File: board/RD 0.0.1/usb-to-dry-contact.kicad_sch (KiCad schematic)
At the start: 11 parts, among them J1 480-37-1000, U1 CP2102N-Axx-xQFN28

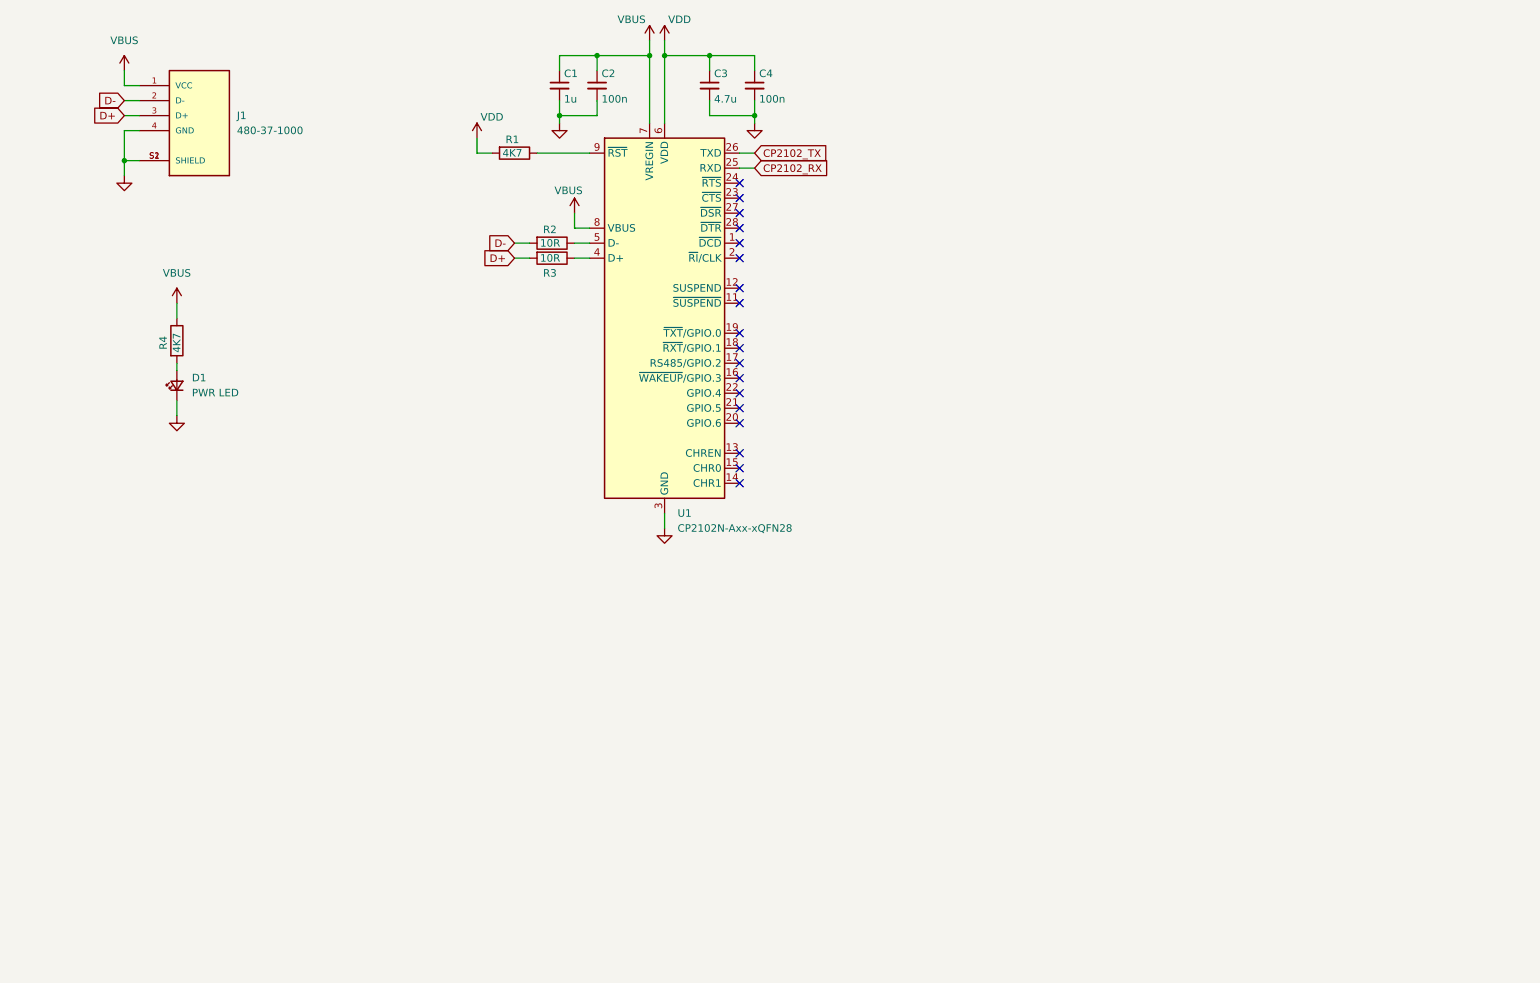
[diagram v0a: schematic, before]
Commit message: add relay, output conn, isp conn, avalanche diode
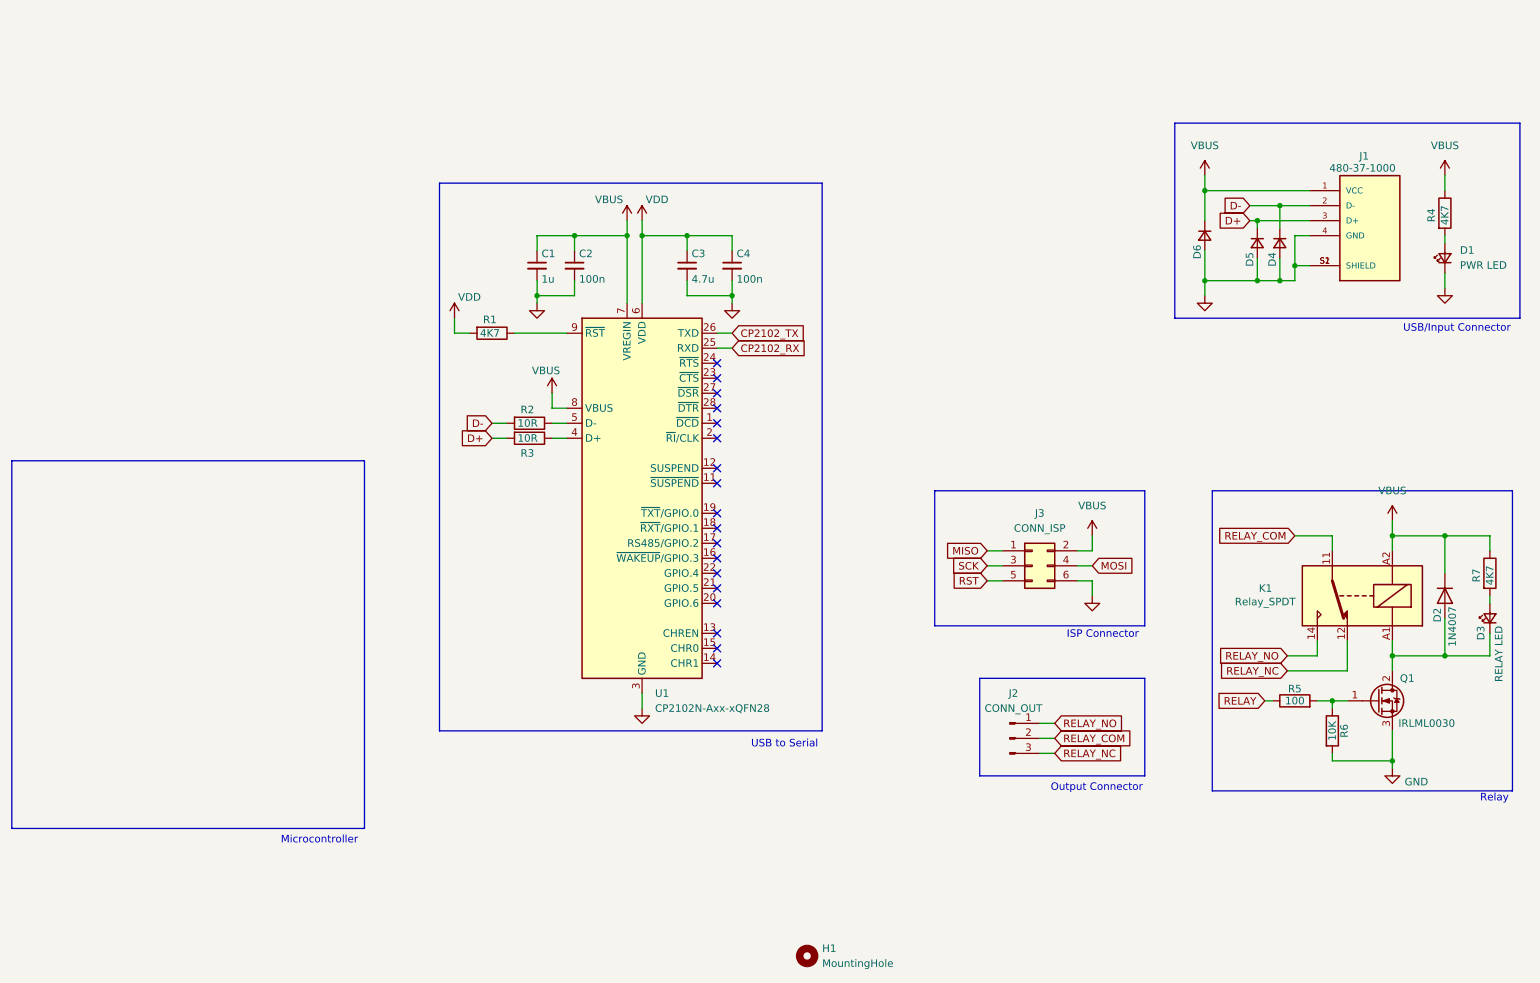
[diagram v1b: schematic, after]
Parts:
- added D2: 1N4007, Diode_SMD:D_SOD-123F, symbol Device:D
- added D3: RELAY LED, symbol Device:LED_Small
- added D4, D5, D6: D_Small, symbol Device:D_Small
- added H1: MountingHole, symbol Mechanical:MountingHole
- added J2: CONN_OUT, symbol Connector:Conn_01x03_Pin
- added J3: CONN_ISP, symbol Connector_Generic:Conn_02x03_Odd_Even
- added K1: Relay_SPDT, symbol Relay:Relay_SPDT
- added Q1: IRLML0030, Package_TO_SOT_SMD:SOT-23, symbol Transistor_FET:IRF540N
- added R5: 100, Resistor_SMD:R_0603_1608Metric_Pad0.98x0.95mm_HandSolder, symbol Device:R
- added R6: 10K, Resistor_SMD:R_0603_1608Metric_Pad0.98x0.95mm_HandSolder, symbol Device:R
- added R7: 4K7, symbol Device:R
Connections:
- net D+: now also D5.1 (K)
- net D-: now also D4.1 (K)
- net GND: now also D4.2 (A), D5.2 (A), D6.2 (A), J3.6 (Pin_6), Q1.3 (S), R6.2
- net VBUS: now also D2.1 (K), D6.1 (K), J3.2 (Pin_2), K1.A2, R7.1
- new net: Q1.1 (G), R5.2, R6.1
- new net: D2.2 (A), D3.1 (K), K1.A1, Q1.2 (D)
- new net: D3.2 (A), R7.2
- new net MISO: J3.1 (Pin_1)
- new net MOSI: J3.4 (Pin_4)
- new net RELAY: R5.1
- new net RELAY_COM: J2.2 (Pin_2), K1.11
- new net RELAY_NC: J2.3 (Pin_3), K1.12
- new net RELAY_NO: J2.1 (Pin_1), K1.14
- new net RST: J3.5 (Pin_5)
- new net SCK: J3.3 (Pin_3)
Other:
- note added: "ISP Connector"
- note added: "Microcontroller"
- note added: "Output Connector"
- note added: "Relay"
- note added: "USB to Serial"
- note added: "USB/Input Connector"
- moved on the sheet: C1, C2, C3, C4, D1, J1, R1, R2, R3, R4, U1

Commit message: add STM8 to sch, change the ISP to SWIM connector, place components to board
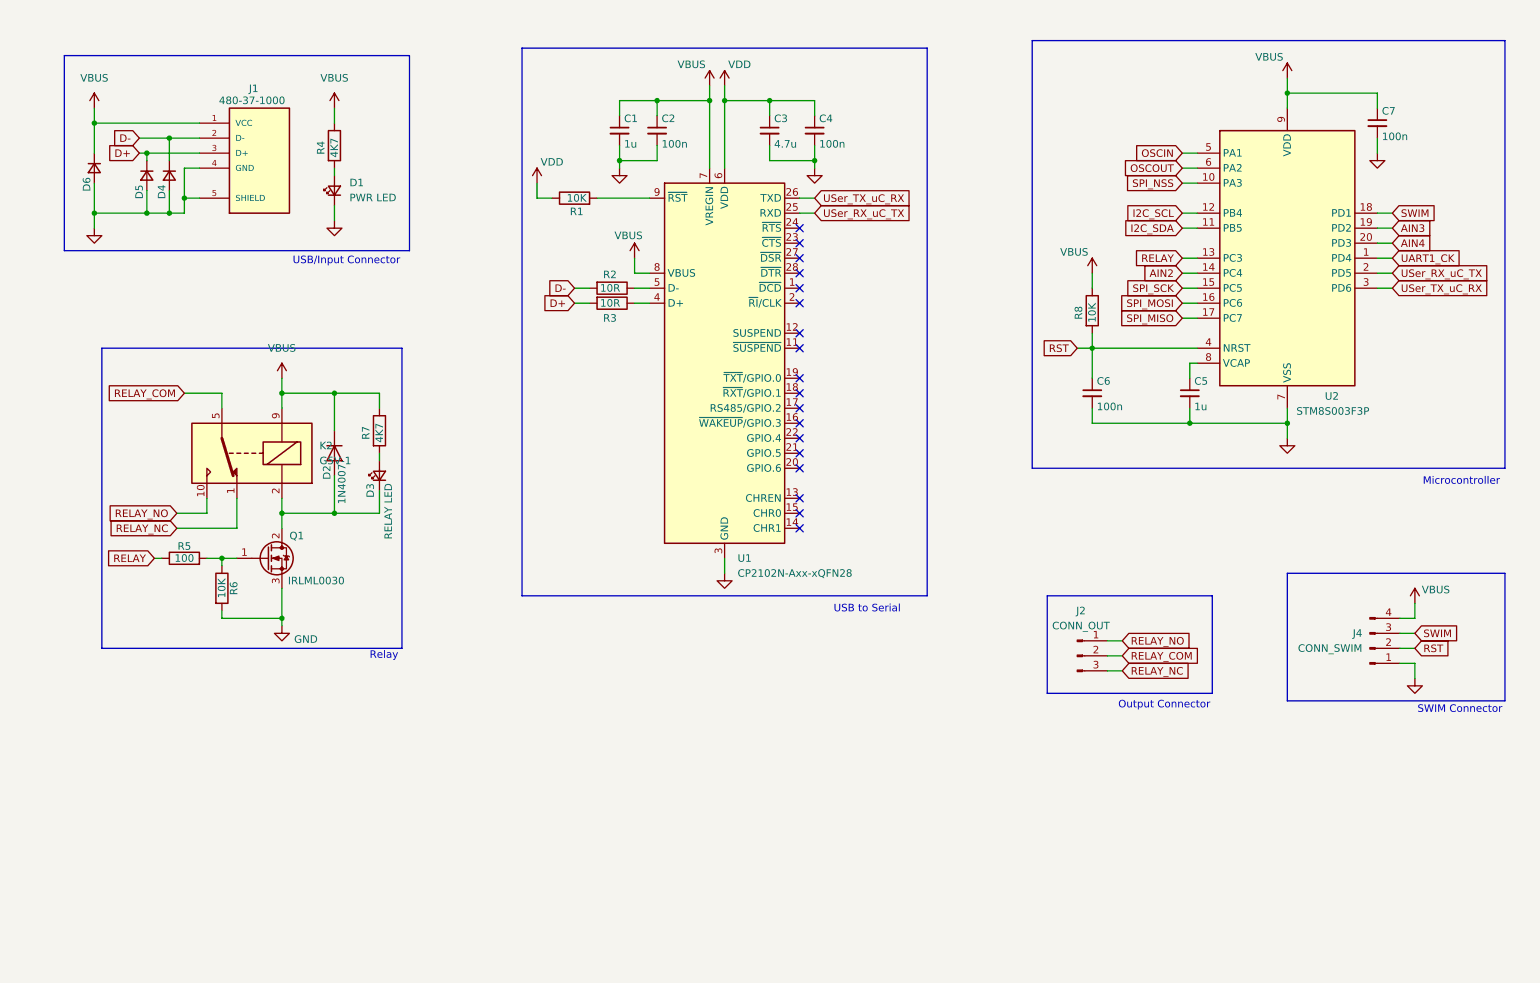
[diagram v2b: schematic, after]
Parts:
- removed H1: MountingHole, symbol Mechanical:MountingHole
- removed J3: CONN_ISP, symbol Connector_Generic:Conn_02x03_Odd_Even
- removed K1: Relay_SPDT, symbol Relay:Relay_SPDT
- added C5: 1u, Capacitor_SMD:C_0603_1608Metric_Pad1.08x0.95mm_HandSolder, symbol Device:C_Small
- added C6, C7: 100n, Capacitor_SMD:C_0603_1608Metric_Pad1.08x0.95mm_HandSolder, symbol Device:C_Small
- added J4: CONN_SWIM, Connector_PinHeader_2.54mm:PinHeader_1x04_P2.54mm_Vertical, symbol Connector:Conn_01x04_Pin
- added K2: G5V-1, Relay_THT:Relay_SPDT_Omron_G5V-1, symbol Relay:G5V-1
- added R8: 10K, Resistor_SMD:R_0603_1608Metric_Pad0.98x0.95mm_HandSolder, symbol Device:R
- added U2: STM8S003F3P, Package_SO:TSSOP-20_4.4x6.5mm_P0.65mm, symbol MCU_ST_STM8:STM8S003F3P
- C1: footprint (none) -> Capacitor_SMD:C_0603_1608Metric_Pad1.08x0.95mm_HandSolder; LCSC Part # (none) -> C14664; Mfg PN (none) -> CC0603KRX5R8BB105
- C2, C4: footprint (none) -> Capacitor_SMD:C_0603_1608Metric_Pad1.08x0.95mm_HandSolder; LCSC Part # (none) -> C14663; Mfg PN (none) -> CC0603KRX7R9BB104
- C3: footprint (none) -> Capacitor_SMD:C_0603_1608Metric_Pad1.08x0.95mm_HandSolder; LCSC Part # (none) -> C277476; Mfg PN (none) -> CC0603KRX5R7BB475
- D1, D3: footprint (none) -> LED_SMD:LED_0603_1608Metric_Pad1.05x0.95mm_HandSolder; LCSC Part # (none) -> C125093; Mfg PN (none) -> LTST-C190GKT
- D4, D5, D6: footprint (none) -> Diode_SMD:D_SOD-123F; LCSC Part # (none) -> C2902912; Mfg PN (none) -> 1N4007 A7
- J1: footprint 480-37-1000:MOLEX_480-37-1000 -> Connector_USB:USB_A_Molex_48037-2200_Horizontal; LCSC Part # (none) -> C319178; Mfg PN (none) -> U217-041N-4BV81
- J2: footprint (none) -> TerminalBlock_Phoenix:TerminalBlock_Phoenix_MKDS-1,5-3-5.08_1x03_P5.08mm_Horizontal; LCSC Part # (none) -> C72334; Mfg PN (none) -> WJ500V-5.08-3P
- R1: value 4K7 -> 10K; footprint (none) -> Resistor_SMD:R_0603_1608Metric_Pad0.98x0.95mm_HandSolder; LCSC Part # (none) -> C98220; Mfg PN (none) -> RC0603FR-0710KL
- R2, R3: footprint (none) -> Resistor_SMD:R_0603_1608Metric_Pad0.98x0.95mm_HandSolder; LCSC Part # (none) -> C109318; Mfg PN (none) -> RC0603FR-0710RL
- R4, R7: footprint (none) -> Resistor_SMD:R_0603_1608Metric_Pad0.98x0.95mm_HandSolder; LCSC Part # (none) -> C105428; Mfg PN (none) -> RC0603JR-074K7L
- U1: LCSC Part # (none) -> C6568; Mfg PN (none) -> CP2102-GMR
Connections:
- net GND: now also J1.5 (SHIELD), C5.2, C6.2, C7.2, J4.1 (Pin_1), U2.7 (VSS); no longer J1.S1 (SHIELD), J1.S2 (SHIELD)
- net RELAY: now also U2.13 (PC3)
- net RELAY_COM: now also K2.5, K2.6
- net RELAY_NC: now also K2.1
- net RELAY_NO: now also K2.10
- net RST: now also C6.1, J4.2 (Pin_2), R8.2, U2.4 (NRST)
- net VBUS: now also C7.1, J4.4 (Pin_4), K2.9, R8.1, U2.9 (VDD)
- net VDD: now also R1.1; no longer R1.2
- net at D2.2 (A), D3.1 (K), Q1.2 (D): now also K2.2
- net at U1.9 (~{RST}): now also R1.2; no longer R1.1
- net CP2102_RX renamed USer_RX_uC_TX
- net USer_RX_uC_TX: now also U2.2 (PD5)
- net CP2102_TX renamed USer_TX_uC_RX
- net USer_TX_uC_RX: now also U2.3 (PD6)
- new net: C5.1, U2.8 (VCAP)
- new net AIN2: U2.14 (PC4)
- new net AIN3: U2.19 (PD2)
- new net AIN4: U2.20 (PD3)
- new net I2C_SCL: U2.12 (PB4)
- new net I2C_SDA: U2.11 (PB5)
- new net OSCIN: U2.5 (PA1)
- new net OSCOUT: U2.6 (PA2)
- new net SPI_MISO: U2.17 (PC7)
- new net SPI_MOSI: U2.16 (PC6)
- new net SPI_NSS: U2.10 (PA3)
- new net SPI_SCK: U2.15 (PC5)
- new net SWIM: J4.3 (Pin_3), U2.18 (PD1)
- new net UART1_CK: U2.1 (PD4)
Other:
- note added: "SWIM Connector"
- note removed: "ISP Connector"
- moved on the sheet: C1, C2, C3, C4, D1, D2, D3, D4, D5, D6, J2, Q1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

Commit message: Finish to route the board
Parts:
- D4, D5, D6: value D_Small -> BZT52B5V1S; footprint Diode_SMD:D_SOD-123F -> Diode_SMD:D_SOD-323; LCSC Part # C2902912 -> C19077434; Mfg PN 1N4007 A7 -> BZT52B5V1S
- K2: LCSC Part # (none) -> C28695; Mfg PN (none) -> G5V-1 DC5
- U1: footprint Package_DFN_QFN:QFN-28-1EP_5x5mm_P0.5mm_EP3.1x3.1mm_ThermalVias -> Package_DFN_QFN:QFN-28-1EP_5x5mm_P0.5mm_EP3.1x3.1mm
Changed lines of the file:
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@@
 			)
 		)
-		(property "Value" "D_Small"
+		(property "Value" "BZT52B5V1S"
 			(at 41.91 52.0699 90)
 			(effects
@@
 			)
 		)
-		(property "Footprint" "Diode_SMD:D_SOD-123F"
+		(property "Footprint" "Diode_SMD:D_SOD-323"
 			(at 39.37 50.8 90)
 			(effects
@@
 			)
 		)
-		(property "LCSC Part #" "C2902912"
+		(property "LCSC Part #" "C19077434"
 			(at 39.37 50.8 0)
 			(effects
@@
 			)
 		)
-		(property "Mfg PN" "1N4007 A7"
+		(property "Mfg PN" "BZT52B5V1S"
 			(at 39.37 50.8 0)
 			(effects
@@
 			)
 		)
-		(property "Value" "D_Small"
+		(property "Value" "BZT52B5V1S"
 			(at 45.72 52.0699 90)
 			(effects
@@
 			)
 		)
-		(property "Footprint" "Diode_SMD:D_SOD-123F"
+		(property "Footprint" "Diode_SMD:D_SOD-323"
 			(at 43.18 50.8 90)
 			(effects
@@
 			)
 		)
-		(property "LCSC Part #" "C2902912"
+		(property "LCSC Part #" "C19077434"
 			(at 43.18 50.8 0)
 			(effects
@@
 			)
 		)
-		(property "Mfg PN" "1N4007 A7"
+		(property "Mfg PN" "BZT52B5V1S"
 			(at 43.18 50.8 0)
 			(effects
@@
 			)
 		)
-		(property "Footprint" "Package_DFN_QFN:QFN-28-1EP_5x5mm_P0.5mm_EP3.1x3.1mm_ThermalVias"
+		(property "Footprint" "Package_DFN_QFN:QFN-28-1EP_5x5mm_P0.5mm_EP3.1x3.1mm"
 			(at 170.18 114.3 0)
 			(effects
@@
 			)
 		)
-		(property "Value" "D_Small"
+		(property "Value" "BZT52B5V1S"
 			(at 33.02 50.7999 90)
 			(effects
@@
 			)
 		)
-		(property "Footprint" "Diode_SMD:D_SOD-123F"
+		(property "Footprint" "Diode_SMD:D_SOD-323"
 			(at 30.48 49.53 90)
 			(effects
@@
 			)
 		)
-		(property "LCSC Part #" "C2902912"
+		(property "LCSC Part #" "C19077434"
 			(at 30.48 49.53 0)
 			(effects
@@
 			)
 		)
-		(property "Mfg PN" "1N4007 A7"
+		(property "Mfg PN" "BZT52B5V1S"
 			(at 30.48 49.53 0)
 			(effects
@@
 			(at 57.15 97.79 0)
 			(effects
+				(font
+					(size 1.27 1.27)
+				)
+				(hide yes)
+			)
+		)
+		(property "LCSC Part #" "C28695"
+			(at 57.15 97.79 0)
+			(effects
+				(font
+					(size 1.27 1.27)
+				)
+				(hide yes)
+			)
+		)
+		(property "Mfg PN" "G5V-1 DC5"
+			(at 57.15 97.79 0)
+			(effects
